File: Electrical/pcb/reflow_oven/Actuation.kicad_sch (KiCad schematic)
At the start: 0 parts

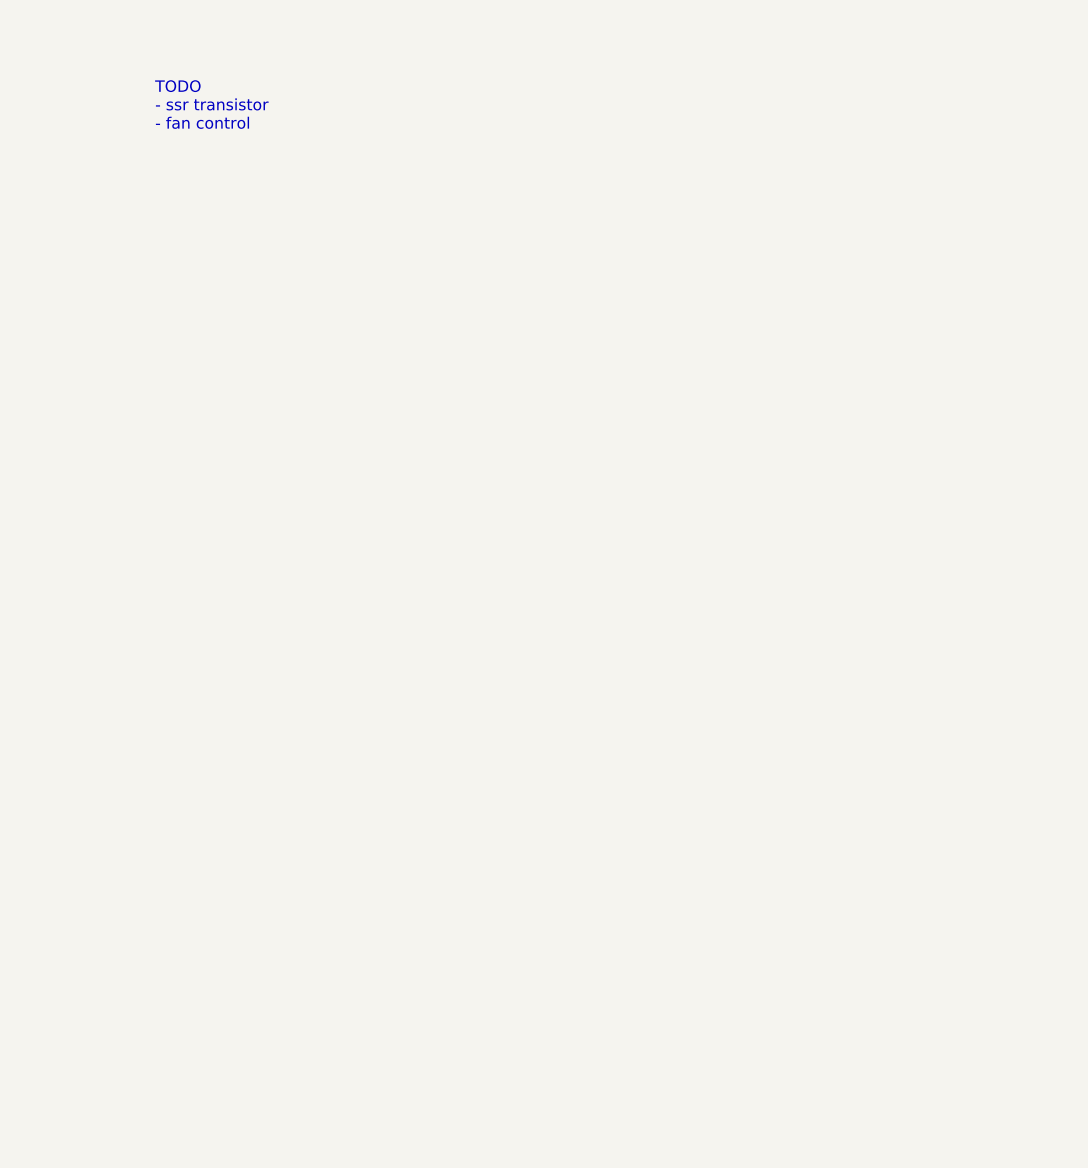
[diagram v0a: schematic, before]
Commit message: functionality
done output stage
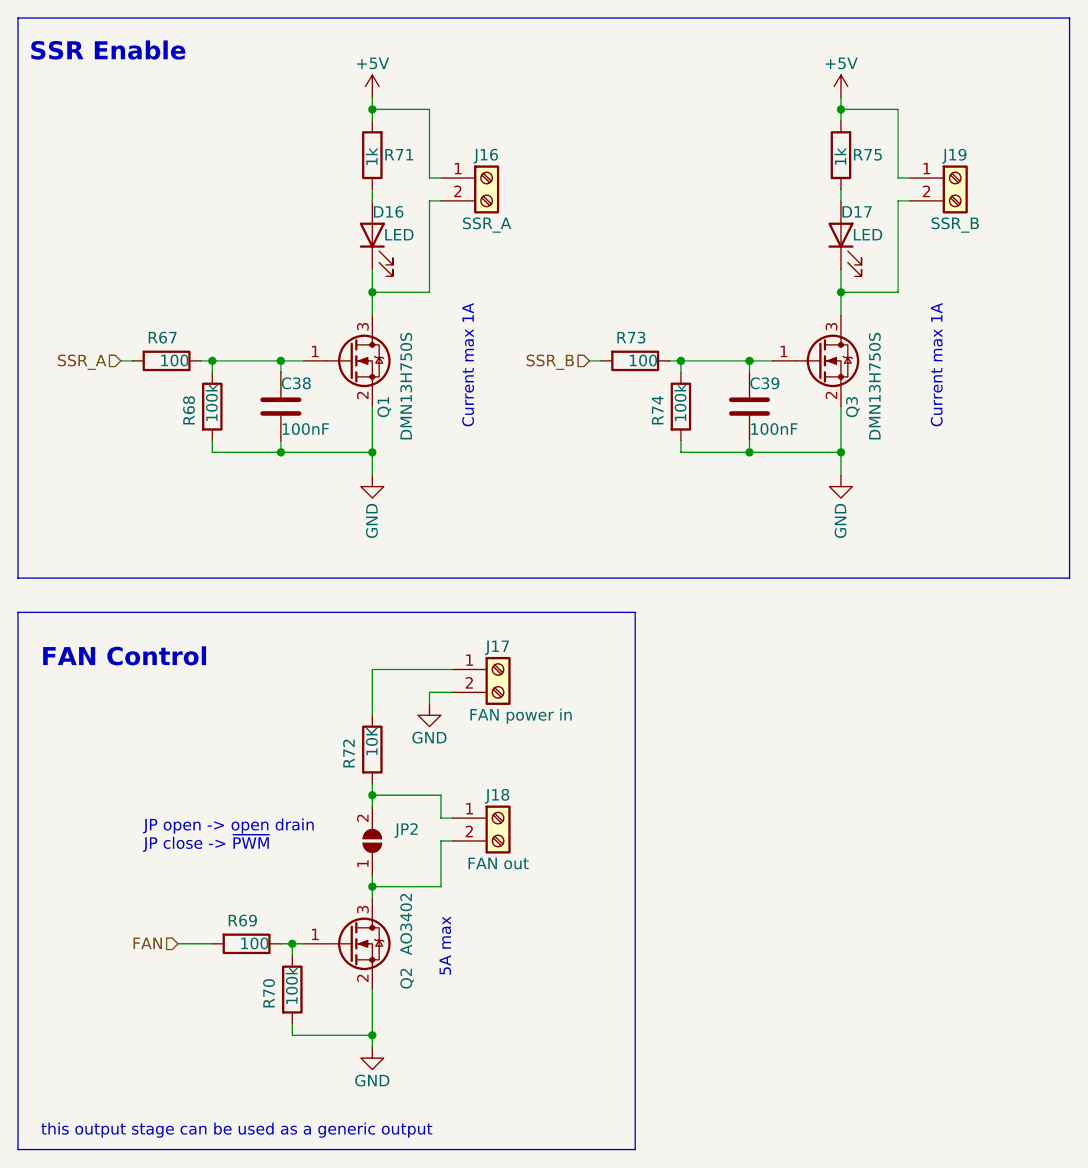
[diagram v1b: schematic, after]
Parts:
- added C38, C39: 100nF, Capacitor_SMD:C_0603_1608Metric, symbol Device:C
- added D16, D17: LED, LED_SMD:LED_0603_1608Metric, symbol Device:LED
- added J16: SSR_A, TerminalBlock_Phoenix:TerminalBlock_Phoenix_MPT-0,5-2-2.54_1x02_P2.54mm_Horizontal, symbol Connector:Screw_Terminal_01x02
- added J17: FAN power in, TerminalBlock_Phoenix:TerminalBlock_Phoenix_MPT-0,5-2-2.54_1x02_P2.54mm_Horizontal, symbol Connector:Screw_Terminal_01x02
- added J18: FAN out, TerminalBlock_Phoenix:TerminalBlock_Phoenix_MPT-0,5-2-2.54_1x02_P2.54mm_Horizontal, symbol Connector:Screw_Terminal_01x02
- added J19: SSR_B, TerminalBlock_Phoenix:TerminalBlock_Phoenix_MPT-0,5-2-2.54_1x02_P2.54mm_Horizontal, symbol Connector:Screw_Terminal_01x02
- added JP2: SolderJumper_2_Open, Jumper:SolderJumper-2_P1.3mm_Open_RoundedPad1.0x1.5mm, symbol Jumper:SolderJumper_2_Open
- added Q1, Q3: DMN13H750S, Package_TO_SOT_SMD:SOT-23, symbol Transistor_FET:DMN13H750S
- added Q2: AO3402, Package_TO_SOT_SMD:SOT-23, symbol Transistor_FET:DMN13H750S
- added R67, R69, R73: 100, Resistor_SMD:R_0603_1608Metric, symbol Device:R
- added R68, R70, R74: 100k, Resistor_SMD:R_0603_1608Metric, symbol Device:R
- added R71, R75: 1k, Resistor_SMD:R_0603_1608Metric, symbol Device:R
- added R72: 10K, Resistor_SMD:R_0603_1608Metric, symbol Device:R
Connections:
- new net: C38.1, Q1.1 (G), R67.1, R68.1
- new net: J18.2 (Pin_2), JP2.1 (A), Q2.3 (D)
- new net: J18.1 (Pin_1), JP2.2 (B), R72.2
- new net: C39.1, Q3.1 (G), R73.1, R74.1
- new net: D16.1 (K), J16.2 (Pin_2), Q1.3 (D)
- new net: J17.1 (Pin_1), R72.1
- new net: D17.1 (K), J19.2 (Pin_2), Q3.3 (D)
- new net: D17.2 (A), R75.1
- new net: Q2.1 (G), R69.1, R70.1
- new net: D16.2 (A), R71.1
- new net +5V: J16.1 (Pin_1), J19.1 (Pin_1), R71.2, R75.2
- new net FAN: R69.2
- new net GND: C38.2, C39.2, J17.2 (Pin_2), Q1.2 (S), Q2.2 (S), Q3.2 (S), R68.2, R70.2, R74.2
- new net SSR_A: R67.2
- new net SSR_B: R73.2
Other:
- note added: "5A max"
- note added: "Current max 1A"
- note added: "FAN Control"
- note added: "JP open -> open drain JP close -> ~{PWM}"
- note added: "SSR Enable"
- note added: "this output stage can be used as a generic output"
- note removed: "TODO - ssr transistor - fan control"
